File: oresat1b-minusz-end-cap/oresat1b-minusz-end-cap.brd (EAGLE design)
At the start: 105.6 x 105.6 mm, 28 parts, among them U1 TCA9543A-PW, U3 HMC5883L, U4 HMC5883L

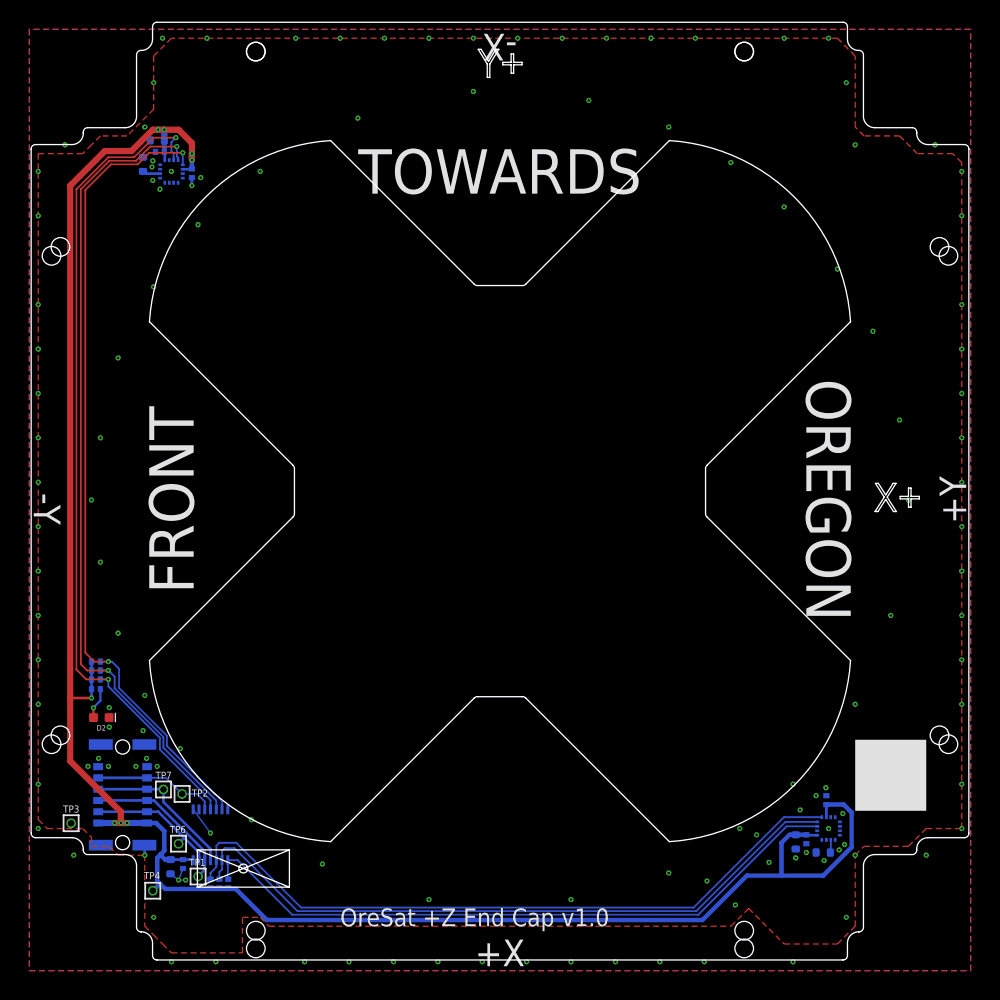
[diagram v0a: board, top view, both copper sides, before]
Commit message: Clean up directory structure to reflect per-satellite end caps
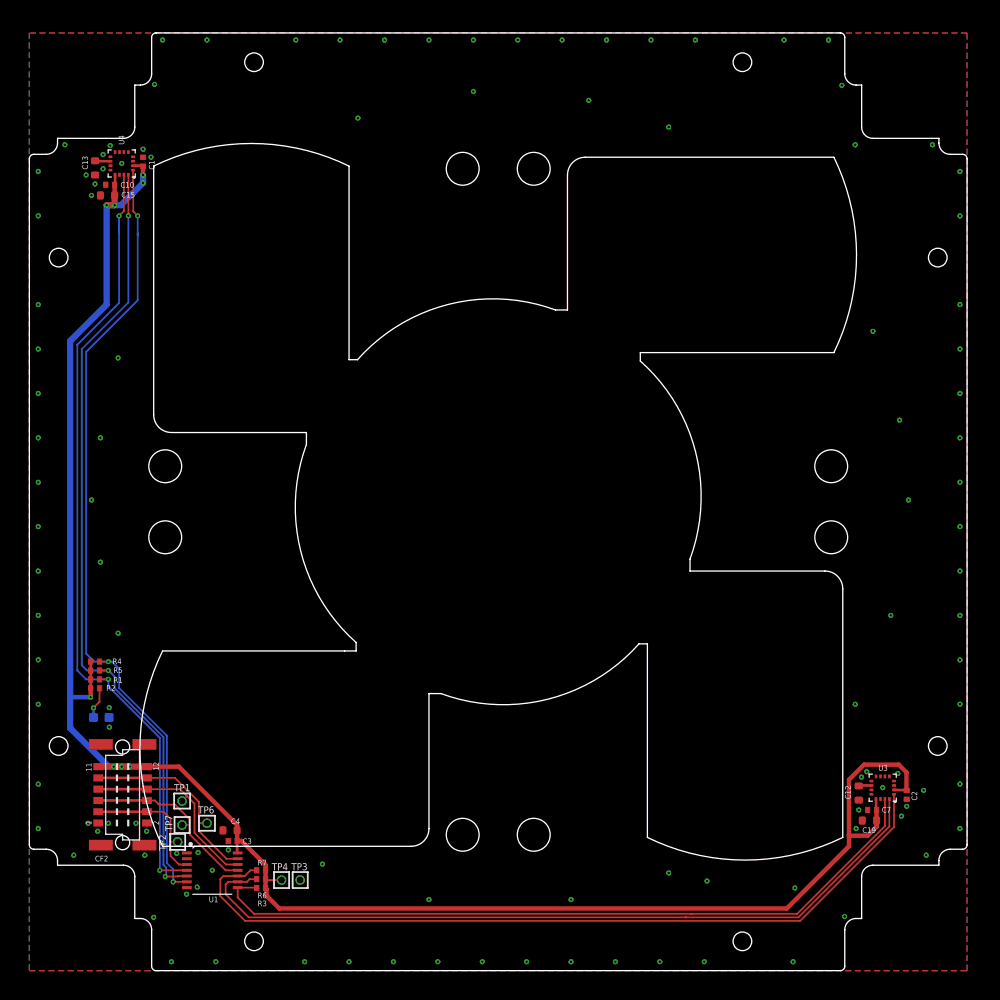
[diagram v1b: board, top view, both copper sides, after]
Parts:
- moved TP3 26.6 mm to (30.5, 10.2)
- moved TP4 14.5 mm to (28.4, 10.2)
- moved C2 9.07 mm to (98.8, 19.8), flipped to the top, turned to 270 degrees
- moved TP1 8.69 mm to (17.2, 19.1), turned to 270 degrees
- moved C19 8.64 mm to (94.6, 16.9), flipped to the top, turned to 180 degrees
- moved C15 8.35 mm to (8.80, 87.3), flipped to the top, turned to 180 degrees
- moved C7 8.10 mm to (94.9, 18.1), flipped to the top, turned to 180 degrees
- moved C4 7.85 mm to (22.6, 15.8), flipped to the top, turned to 180 degrees
- moved C12 7.80 mm to (93.4, 20.0), flipped to the top, turned to 270 degrees
- moved U3 7.64 mm to (96.1, 20.6), flipped to the top, turned to 180 degrees
- moved C10 6.71 mm to (9.10, 88.5), flipped to the top, turned to 180 degrees
- moved C3 6.17 mm to (22.9, 14.6), flipped to the top, turned to 180 degrees
- moved R7 5.89 mm to (26.1, 11.3), flipped to the top, turned to 0 degrees
- moved U4 5.67 mm to (10.4, 90.9), flipped to the top, turned to 180 degrees
- moved C1 5.65 mm to (12.8, 91.1), flipped to the top, turned to 90 degrees
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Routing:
- net 3.3V: track 228.8 -> 213.4 mm
- net SC1: track 79.6 -> 91.5 mm
- net SD1: track 77.6 -> 88.0 mm
- net !INT1: track 75.2 -> 84.1 mm
- net GND: track 8.66 -> 0.00 mm, vias 129 -> 116
- net I2C-SDA: track 15.0 -> 22.3 mm
- net I2C-SCL: track 17.5 -> 21.9 mm
- net I2C-!INT: track 17.5 -> 20.9 mm
- net !INT0: track 94.9 -> 91.8 mm, vias 2 -> 3
- net SDA0: track 92.8 -> 90.0 mm, vias 2 -> 3
- net !I2C-RESET: track 14.0 -> 15.7 mm
- net SCL0: track 92.3 -> 90.7 mm, vias 2 -> 3
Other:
- outline, holes or cut-outs redrawn
- board text added: "OreSat -Z End Cap v1.0"
- board text removed: "FRONT"
- board text removed: "OREGON"
- board text removed: "OreSat +Z End Cap v1.0"
- board text removed: "TOWARDS"
